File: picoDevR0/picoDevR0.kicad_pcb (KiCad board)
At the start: 4 copper layers, 10 parts, among them J1 Barrel_Jack, J2 Pico1to20, SW1 SW_Push_Dual, U1 LM1117-3.3

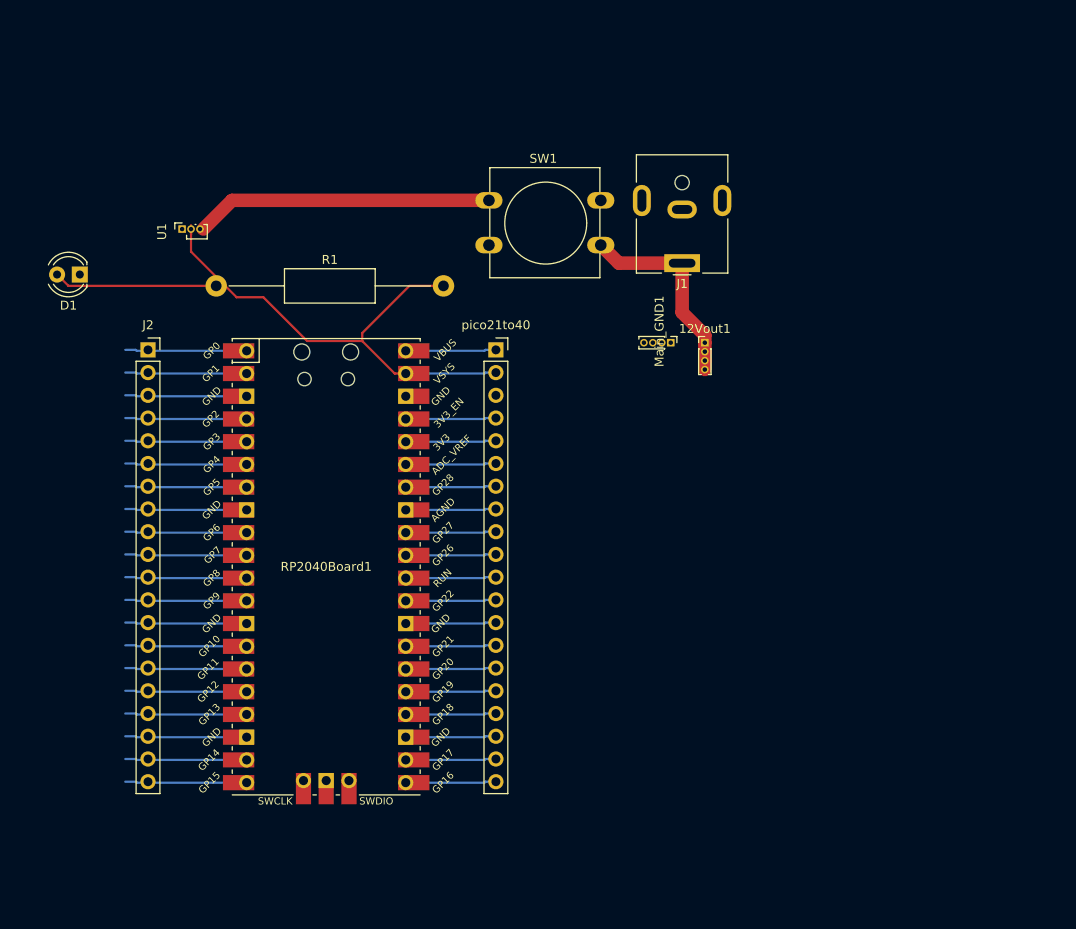
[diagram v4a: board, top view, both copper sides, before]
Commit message: added 5V layer
added everything to the PCB. 
issues: 5V layer is not getting connected with the pico Vcc and the LED resistor for some reason, needs debugging.
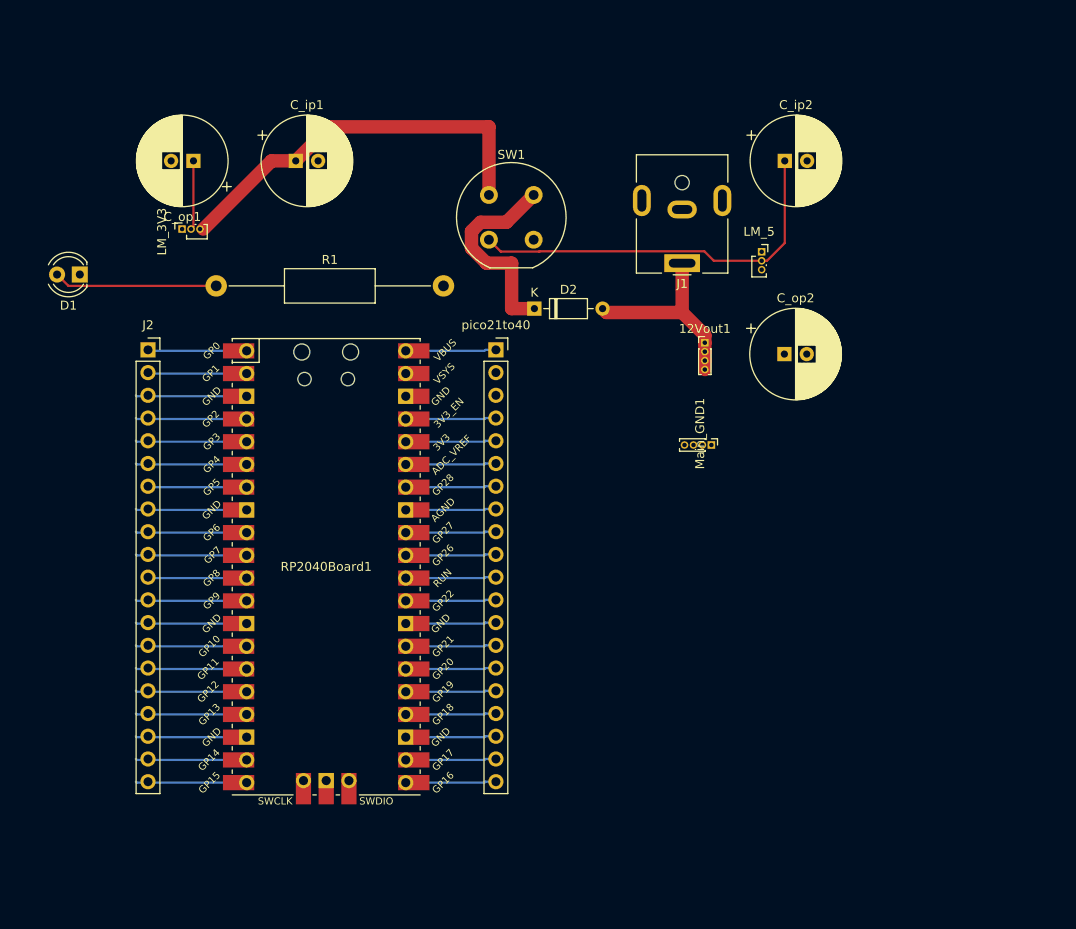
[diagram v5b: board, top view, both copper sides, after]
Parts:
- added C_ip1: C, Capacitor_THT:CP_Radial_D10.0mm_P2.50mm, F.Cu at (116.8, 43.2)
- added C_ip2: C, Capacitor_THT:CP_Radial_D10.0mm_P2.50mm, F.Cu at (171.5, 43.2)
- added C_op1: C, Capacitor_THT:CP_Radial_D10.0mm_P2.50mm, F.Cu at (105.4, 43.2)
- added C_op2: C, Capacitor_THT:CP_Radial_D10.0mm_P2.50mm, F.Cu at (171.4, 64.8)
- added D2: 1N4148, Diode_THT:D_DO-35_SOD27_P7.62mm_Horizontal, F.Cu at (143.5, 59.7)
- added LM_5: LM1117-5.0, Connector_PinSocket_1.00mm:PinSocket_1x03_P1.00mm_Vertical, F.Cu at (168.9, 53.3)
- SW1: footprint Button_Switch_THT:SW_PUSH-12mm -> Button_Switch_THT:Push_E-Switch_KS01Q01
- moved Main_GND1 12.3 mm to (163.3, 74.9)
- moved SW1 0.60 mm to (138.4, 47.0)
- renumbered U1 to LM_3V3
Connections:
- 12Vout1 pad 1: Net-(12Vout1-Pad1) -> +12V
- 12Vout1 pad 2: Net-(12Vout1-Pad1) -> +12V
- 12Vout1 pad 3: Net-(12Vout1-Pad1) -> +12V
- 12Vout1 pad 4: Net-(12Vout1-Pad1) -> +12V
- J1 pad 1: Net-(12Vout1-Pad1) -> +12V
- LM_3V3 pad 2: Net-(R1-Pad2) -> +3V3
- R1 pad 2: Net-(R1-Pad2) -> +5V
- RP2040Board1 pad 39: Net-(R1-Pad2) -> +5V
- SW1 pad 2: Net-(12Vout1-Pad1) -> Net-(D2-Pad1)
- pico21to40 pad 2: Net-(R1-Pad2) -> +5V
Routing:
- net Net-(R1-Pad2): track 55.5 -> 0.00 mm
- net Net-(C_ip2-Pad1): track 0.00 -> 44.1 mm
- net Net-(D2-Pad1): track 0.00 -> 23.3 mm
- net Net-(12Vout1-Pad1): track 22.9 -> 0.00 mm
- net +12V: track 0.00 -> 22.0 mm
- net Net-(C_ip1-Pad1): track 33.2 -> 44.3 mm
- net +3V3: track 0.00 -> 7.73 mm
- net Net-(J2-Pad7): track 13.6 -> 11.1 mm
- net Net-(J2-Pad2): track 13.6 -> 11.1 mm
- net Net-(J2-Pad11): track 13.6 -> 11.1 mm
- net Net-(J2-Pad1): track 13.6 -> 11.1 mm
- net Net-(J2-Pad9): track 13.6 -> 12.4 mm
- net Net-(J2-Pad8): track 13.6 -> 12.4 mm
- net Net-(J2-Pad6): track 13.6 -> 12.4 mm
- net Net-(J2-Pad5): track 13.6 -> 12.4 mm
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- added copper zone on In2.Cu, net +5V

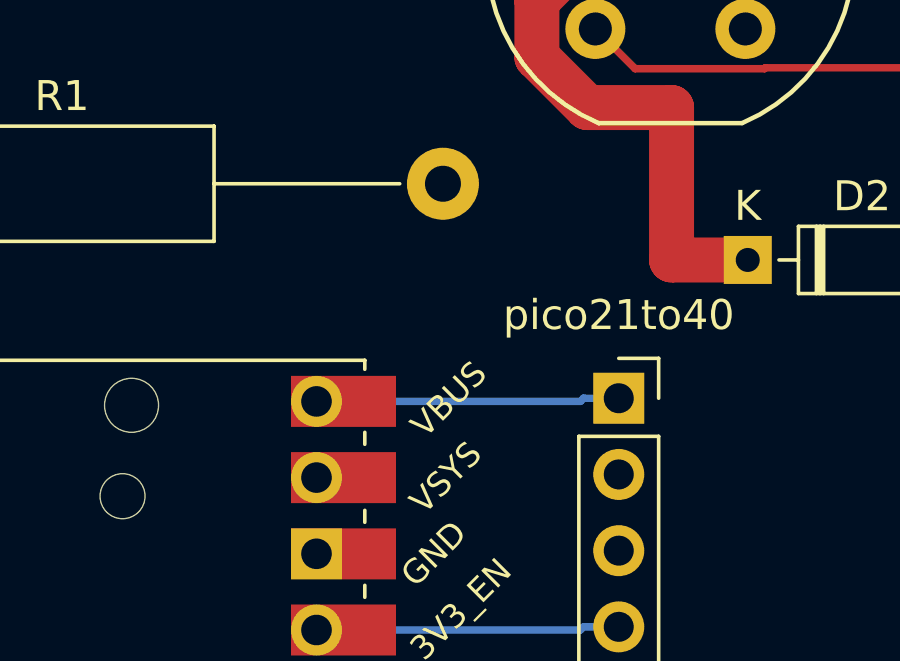
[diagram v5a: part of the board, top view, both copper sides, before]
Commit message: updated README
Updated photos
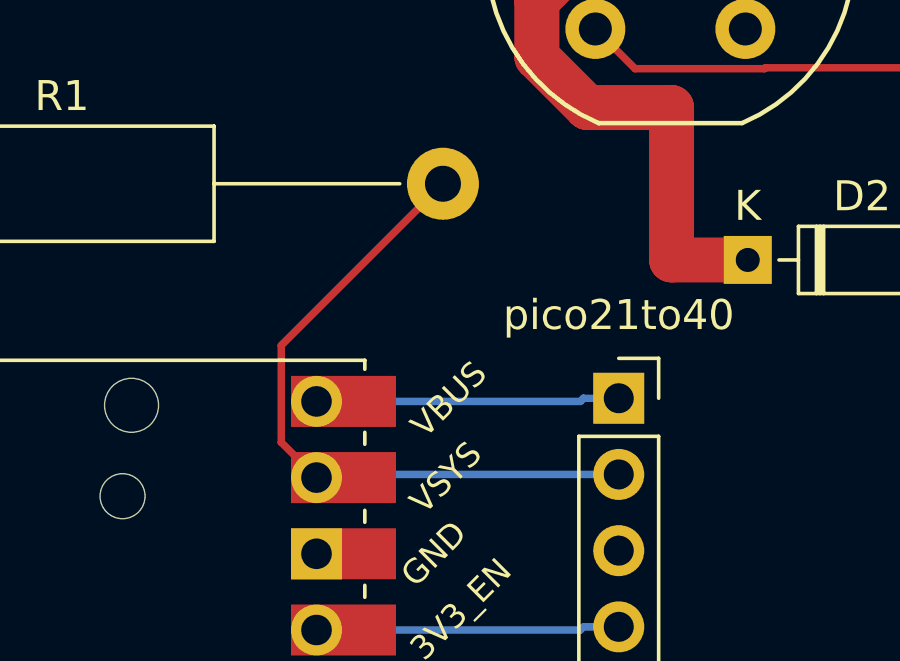
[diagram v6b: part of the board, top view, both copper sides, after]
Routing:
- net +5V: track 0.00 -> 22.6 mm

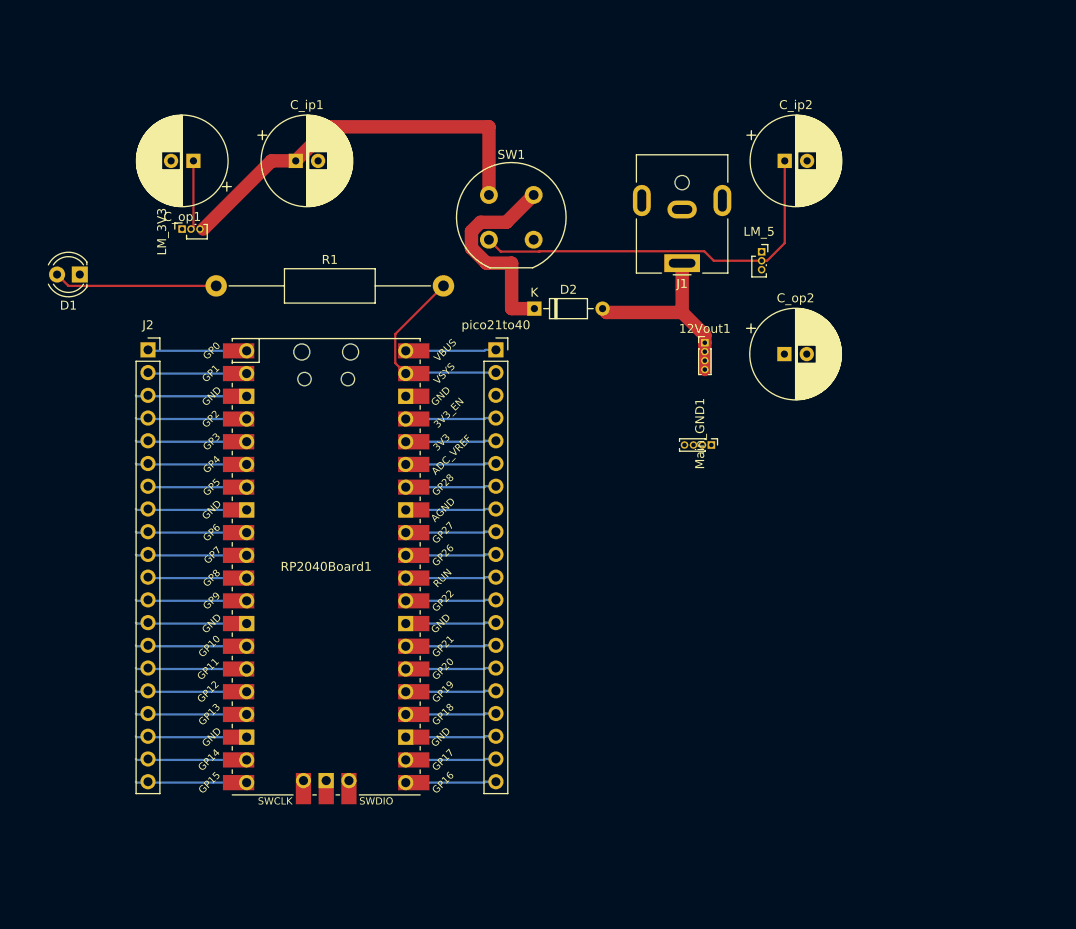
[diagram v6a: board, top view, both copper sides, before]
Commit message: reset everything in the PCB
There were many issues with the earlier approach of constantly making changes in the PCB layer after sch like the 5V layer wasn't being accessed by some pins, and so on. Hence it is decided that henceforth the sch will be first finished and then we shall move on to the PCB design part
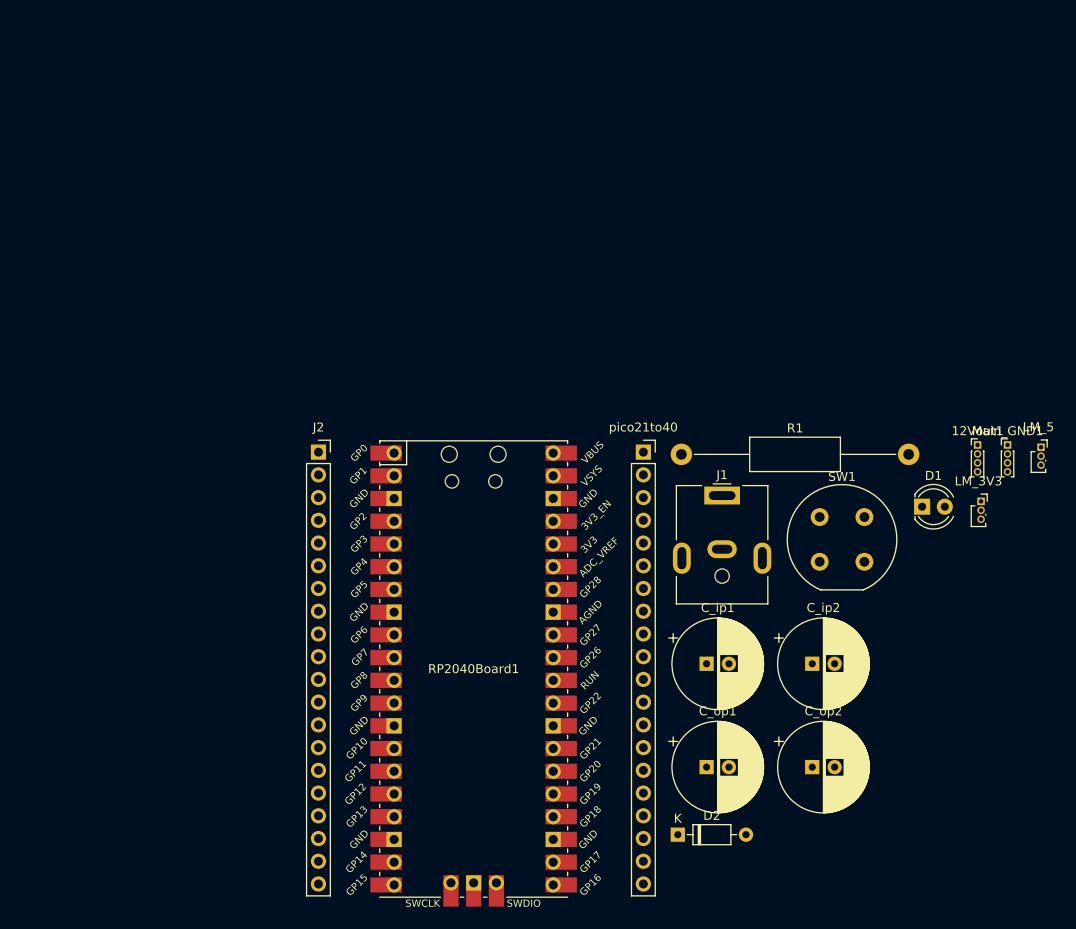
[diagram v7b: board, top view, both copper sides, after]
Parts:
- moved D1 97.6 mm to (186.8, 81.8), turned to 0 degrees
- moved LM_3V3 94.3 mm to (193.4, 81.2), turned to 0 degrees
- moved C_op1 88.8 mm to (162.8, 110.9), turned to 0 degrees
- moved C_ip1 72.6 mm to (162.8, 99.4)
- moved D2 60.9 mm to (159.5, 118.5)
- moved C_ip2 56.3 mm to (174.6, 99.4)
- moved R1 55.3 mm to (159.9, 76.0)
- moved SW1 51.6 mm to (175.4, 83.0)
- moved C_op2 46.3 mm to (174.6, 110.9)
- moved LM_5 38.1 mm to (200.1, 75.2)
- moved Main_GND1 33.1 mm to (196.4, 74.9), turned to 0 degrees
- moved 12Vout1 32.6 mm to (193.0, 74.9)
- moved J1 26.4 mm to (164.5, 80.6), turned to 0 degrees
- moved J2 22.2 mm to (119.4, 75.7)
- moved pico21to40 20.1 mm to (155.7, 75.7)
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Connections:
- SW1 pad 4: Net-(SW1-Pad4) -> +12V
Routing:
- net Net-(C_ip1-Pad1): track 44.3 -> 0.00 mm
- net Net-(C_ip2-Pad1): track 44.1 -> 0.00 mm
- net Net-(D2-Pad1): track 23.3 -> 0.00 mm
- net +5V: track 22.6 -> 0.00 mm
- net +12V: track 22.0 -> 0.00 mm
- net Net-(D1-Pad2): track 18.2 -> 0.00 mm
- net Net-(J2-Pad8): track 12.4 -> 0.00 mm
- net Net-(J2-Pad6): track 12.4 -> 0.00 mm
- net Net-(J2-Pad5): track 12.4 -> 0.00 mm
- net Net-(J2-Pad4): track 12.4 -> 0.00 mm
- net Net-(J2-Pad3): track 12.4 -> 0.00 mm
- net Net-(J2-Pad20): track 12.4 -> 0.00 mm
- net Net-(J2-Pad19): track 12.4 -> 0.00 mm
- net Net-(J2-Pad17): track 12.4 -> 0.00 mm
- net Net-(J2-Pad15): track 12.4 -> 0.00 mm
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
